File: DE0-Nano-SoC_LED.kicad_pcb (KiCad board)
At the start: 2 copper layers, 96.8 x 168.7 mm, 126 parts, among them J1 Conn_02x08_Odd_Even, J10 Conn_01x08, J11 Conn_01x01, J12 Conn_01x01, J13 Conn_01x01, J14 Conn_01x01, J15 Conn_01x01, J16 Conn_01x10, J17 Conn_01x08, J18 Conn_01x01, J19 Conn_01x01, J2 Conn_02x08_Odd_Even, J20 Conn_02x08_Odd_Even, J21 Conn_02x08_Odd_Even, J22 Conn_02x08_Odd_Even, J23 Conn_02x08_Odd_Even, J24 Conn_02x08_Odd_Even, J3 Conn_02x20_Odd_Even, J4 Conn_02x20_Odd_Even, J5 Conn_02x08_Odd_Even, J6 Conn_02x08_Odd_Even, J7 Conn_02x08_Odd_Even, J8 Conn_01x01, J9 Conn_01x06, U1 74HC245, U10 74HC245, U11 74HC245, U12 74HC245, U13 74HC245, U14 74HC245, U15 74HC245, U16 74HC245, U17 74HC245, U18 74HC245, U19 74HC245, U2 74HC245, U20 74HC245, U3 74HC245, U4 74HC245, U5 74HC245, U6 74HC245, U7 74HC245, U8 74HC245, U9 74HC245

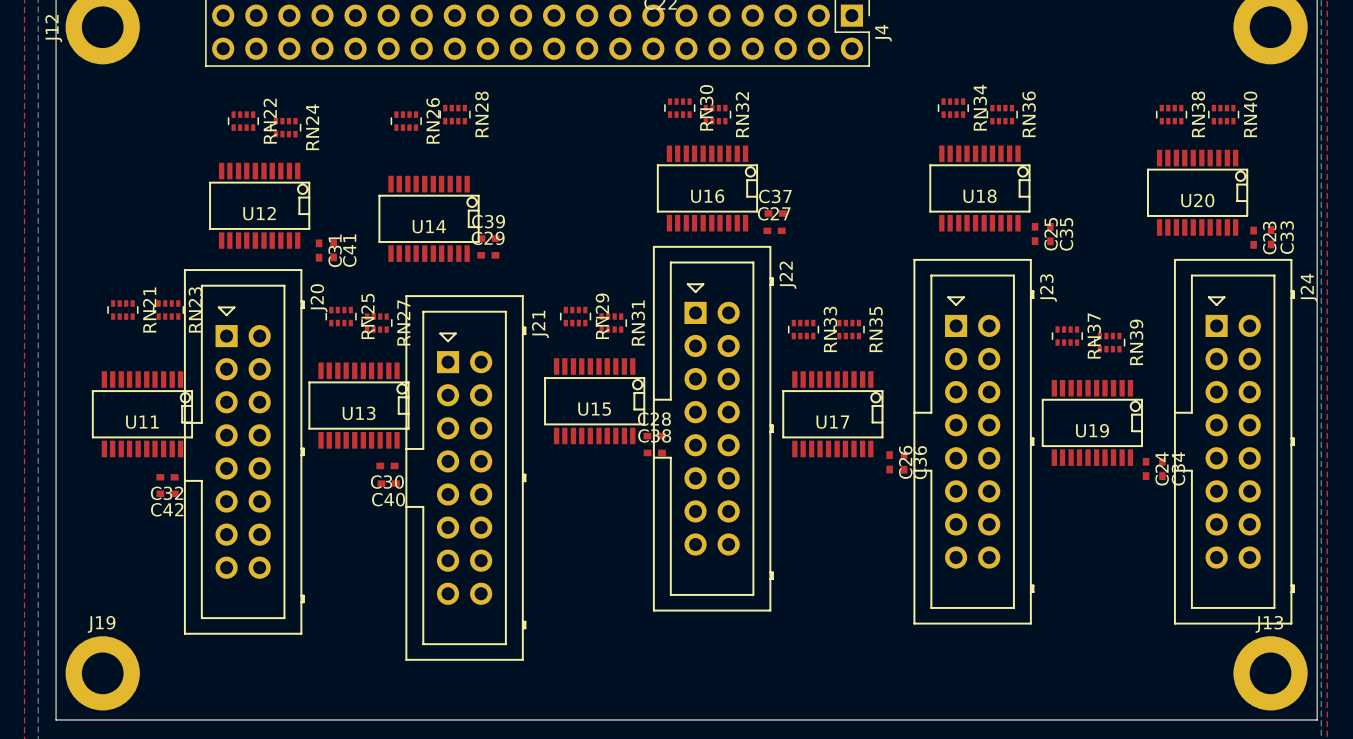
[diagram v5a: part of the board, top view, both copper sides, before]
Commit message: parts autoalign works! (not worth it)
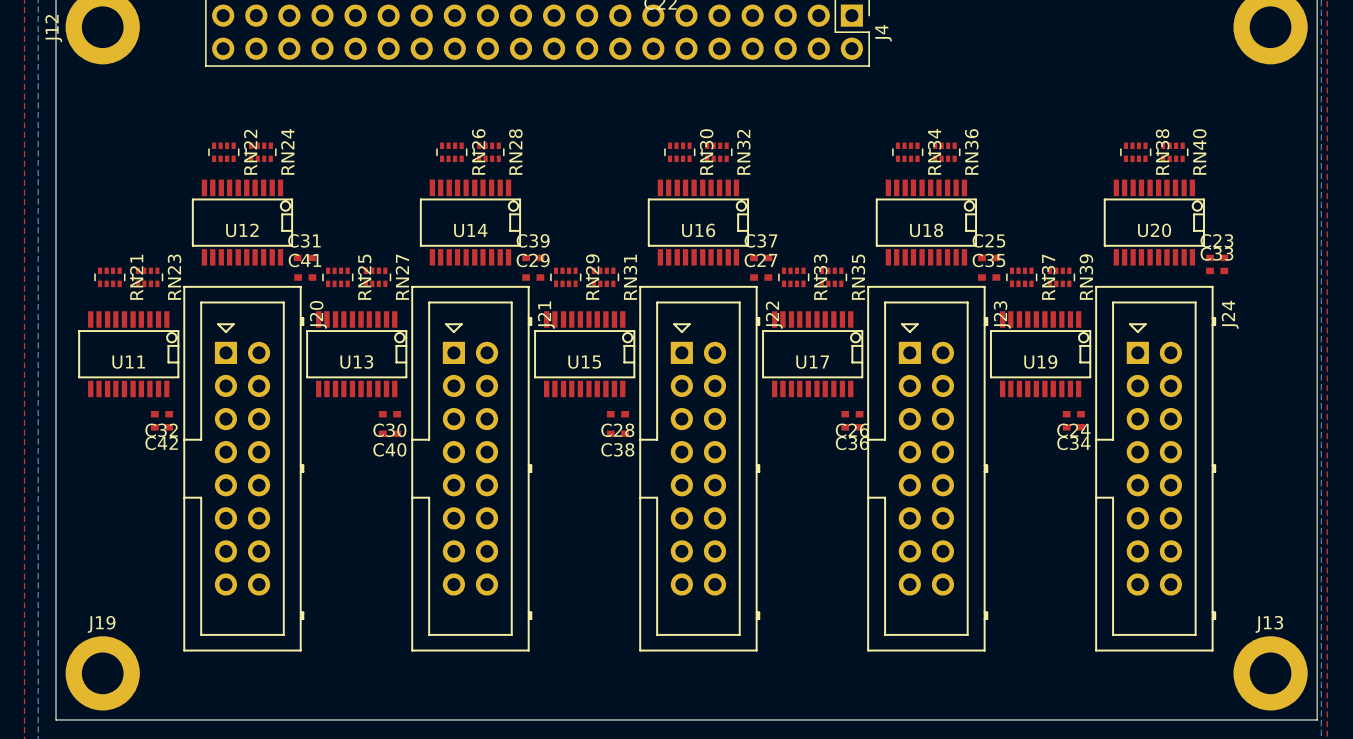
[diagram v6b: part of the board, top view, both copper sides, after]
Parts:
- moved C34 7.52 mm to (144.6, 162.9), turned to 180 degrees
- moved C24 6.95 mm to (144.6, 161.9), turned to 180 degrees
- moved U19 6.60 mm to (142.0, 157.3)
- moved J24 6.39 mm to (149.5, 157.2)
- moved RN39 6.32 mm to (143.4, 151.4)
- moved C35 5.76 mm to (138.1, 151.4), turned to 0 degrees
- moved RN37 5.71 mm to (140.6, 151.4)
- moved RN36 5.26 mm to (134.7, 141.8)
- moved C42 5.12 mm to (74.5, 162.9)
- moved C33 4.88 mm to (155.6, 150.9), turned to 0 degrees
- moved RN34 4.87 mm to (131.8, 141.8)
- moved U18 4.87 mm to (133.2, 147.2)
- moved U17 4.86 mm to (124.5, 157.3)
- moved C32 4.86 mm to (74.5, 161.9)
- moved RN40 4.85 mm to (152.2, 141.8)
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
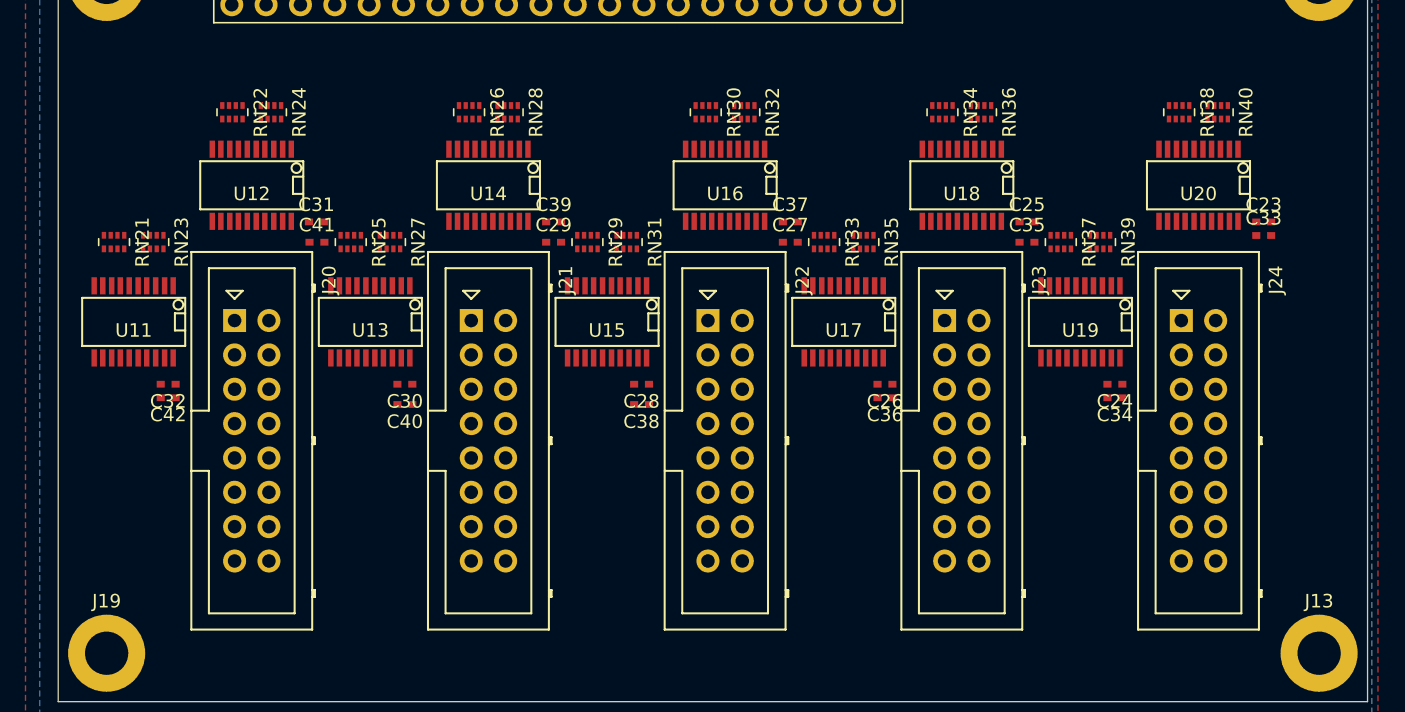
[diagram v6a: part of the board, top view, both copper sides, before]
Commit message: parts auto align was a stupid idea
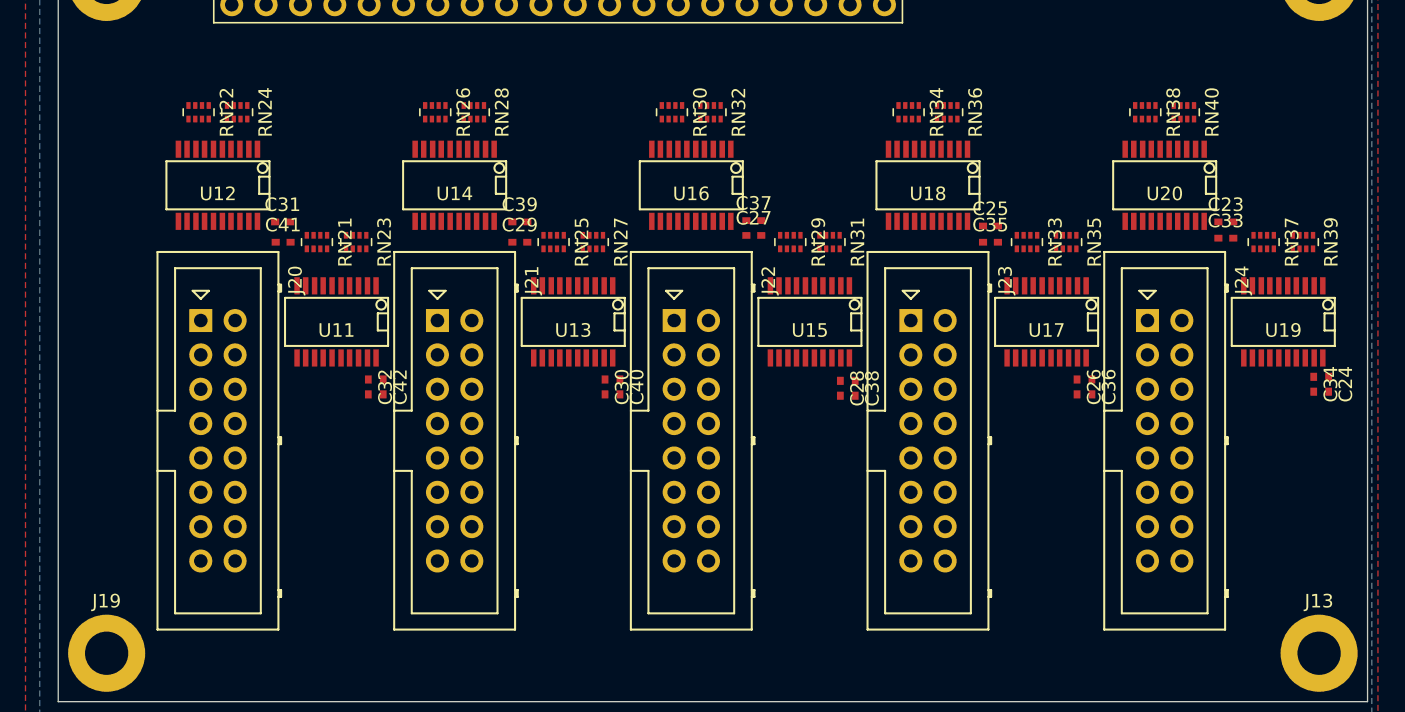
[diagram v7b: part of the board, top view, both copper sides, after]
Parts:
- moved C40 16.0 mm to (108.0, 162.1), turned to 270 degrees
- moved C42 15.9 mm to (90.5, 162.1), turned to 270 degrees
- moved C38 15.8 mm to (125.3, 162.2), turned to 270 degrees
- moved C24 15.8 mm to (160.3, 161.9), turned to 270 degrees
- moved C36 15.3 mm to (142.8, 162.1), turned to 270 degrees
- moved RN33 15.0 mm to (138.1, 151.4)
- moved RN21 15.0 mm to (85.5, 151.4)
- moved RN23 15.0 mm to (88.5, 151.4)
- moved RN25 15.0 mm to (103.0, 151.4)
- moved RN27 15.0 mm to (106.0, 151.4)
- moved RN29 15.0 mm to (120.5, 151.4)
- moved RN31 15.0 mm to (123.5, 151.4)
- moved RN37 15.0 mm to (155.6, 151.4)
- moved RN39 15.0 mm to (158.4, 151.4)
- moved U11 15.0 mm to (87.0, 157.3)
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
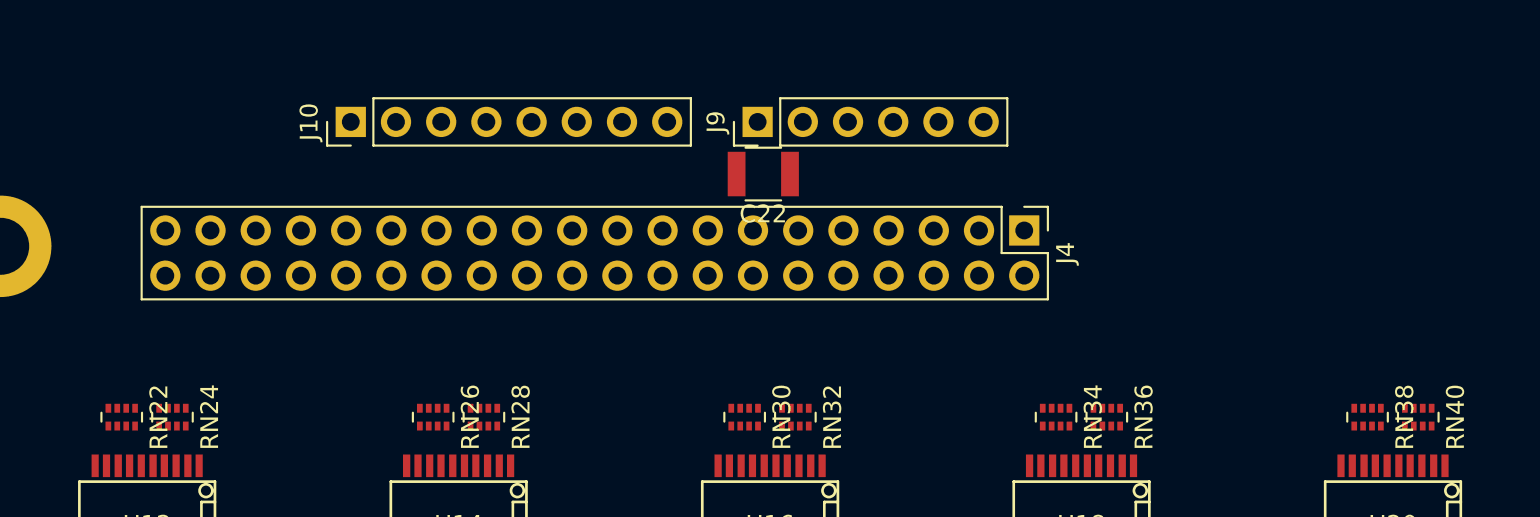
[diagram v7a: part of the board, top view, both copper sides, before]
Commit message: pin swapping
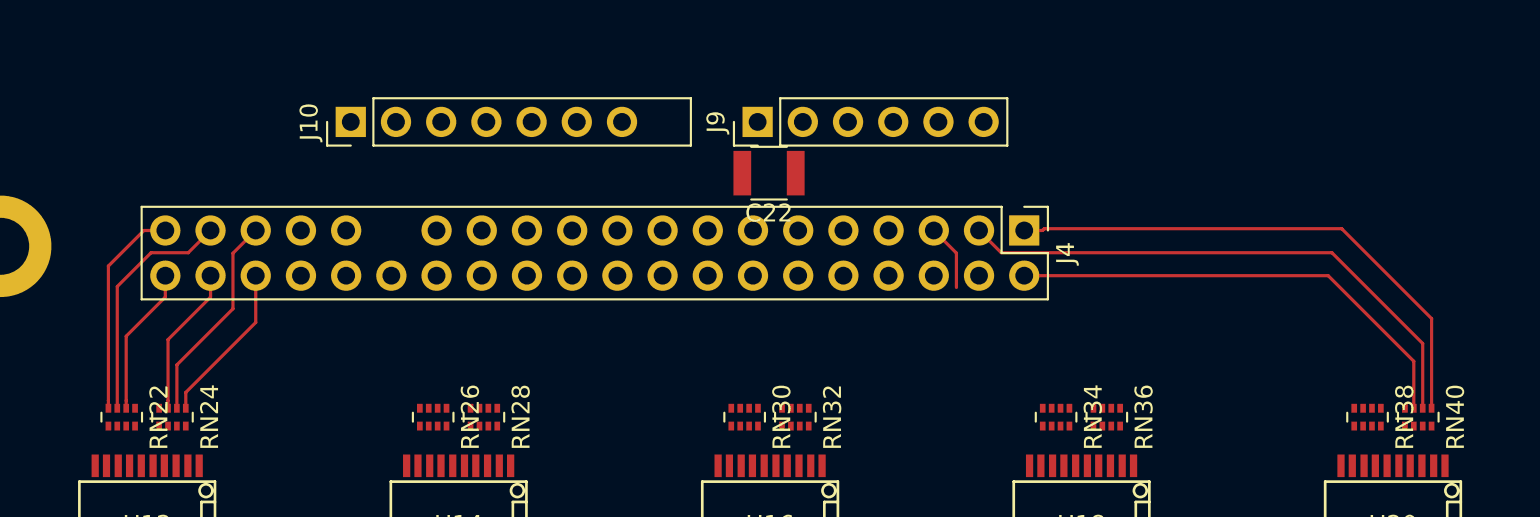
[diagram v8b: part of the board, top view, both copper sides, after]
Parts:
- moved C22 0.32 mm to (113.2, 128.1)
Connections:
- J4 pad 15: /CLK__2 -> /G1_8
- J4 pad 16: /LAT__2 -> /B1_8
- J4 pad 17: /C__2 -> /R1_8
- J4 pad 18: /D__2 -> /R2_8
- J4 pad 19: /A__2 -> /G2_8
- J4 pad 2: /B1_6 -> /R1_6
- J4 pad 20: /B__2 -> /B2_8
- J4 pad 21: /B1_8 -> /CLK__2
- J4 pad 22: /G1_8 -> /LAT__2
- J4 pad 23: /R2_8 -> /C__2
- J4 pad 24: /R1_8 -> /D__2
- J4 pad 25: /B2_8 -> /A__2
- J4 pad 26: /G2_8 -> /B__2
- J4 pad 3: /R1_6 -> /B1_6
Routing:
- net /B1_6: track 0.00 -> 31.2 mm
- net /G1_6: track 0.00 -> 30.1 mm
- net /R1_6: track 0.00 -> 26.5 mm
- net /G2_10: track 0.00 -> 13.4 mm
- net /B2_10: track 0.00 -> 12.0 mm
- net /B1_10: track 0.00 -> 11.8 mm
- net /G1_10: track 0.00 -> 9.08 mm
- net /R1_10: track 0.00 -> 8.44 mm
- net /R2_10: track 0.00 -> 8.36 mm
- net /G2_6: track 0.00 -> 3.73 mm
